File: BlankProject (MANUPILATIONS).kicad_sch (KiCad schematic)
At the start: 10 parts

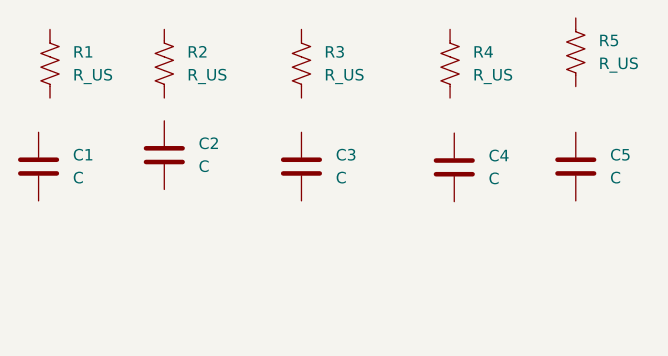
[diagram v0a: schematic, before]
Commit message: Resistance libraries changed.
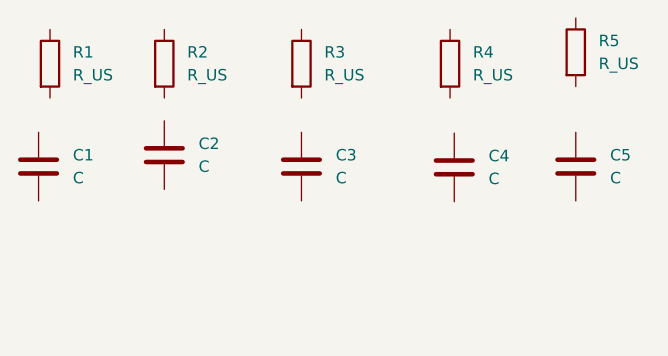
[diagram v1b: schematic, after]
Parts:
- R1, R2, R3, R4, R5: symbol Device:R_US -> Device:R
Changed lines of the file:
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@@
 	(paper "A4")
 	(symbol
-		(lib_id "Device:R_US")
+		(lib_id "Device:R")
 		(at 156.21 77.47 0)
 		(unit 1)
@@
 			)
 		)
-		(property "Description" "Resistor, US symbol"
+		(property "Description" "Resistor"
 			(at 156.21 77.47 0)
 			(effects
@@
 	)
 	(symbol
-		(lib_id "Device:R_US")
+		(lib_id "Device:R")
 		(at 142.24 78.74 0)
 		(unit 1)
@@
 			)
 		)
-		(property "Description" "Resistor, US symbol"
+		(property "Description" "Resistor"
 			(at 142.24 78.74 0)
 			(effects
@@
 	)
 	(symbol
-		(lib_id "Device:R_US")
+		(lib_id "Device:R")
 		(at 125.73 78.74 0)
 		(unit 1)
@@
 			)
 		)
-		(property "Description" "Resistor, US symbol"
+		(property "Description" "Resistor"
 			(at 125.73 78.74 0)
 			(effects
@@
 	)
 	(symbol
-		(lib_id "Device:R_US")
+		(lib_id "Device:R")
 		(at 97.79 78.74 0)
 		(unit 1)
@@
 			)
 		)
-		(property "Description" "Resistor, US symbol"
+		(property "Description" "Resistor"
 			(at 97.79 78.74 0)
 			(effects
@@
 	)
 	(symbol
-		(lib_id "Device:R_US")
+		(lib_id "Device:R")
 		(at 110.49 78.74 0)
 		(unit 1)
@@
 			)
 		)
-		(property "Description" "Resistor, US symbol"
+		(property "Description" "Resistor"
 			(at 110.49 78.74 0)
 			(effects

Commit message: Inductors are added.
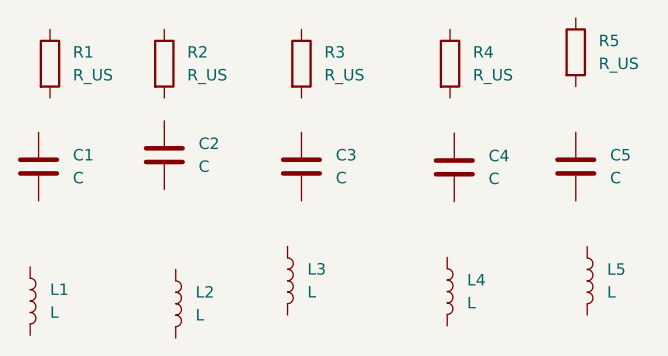
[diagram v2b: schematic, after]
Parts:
- added L1, L2, L3, L4, L5: L, symbol Device:L
